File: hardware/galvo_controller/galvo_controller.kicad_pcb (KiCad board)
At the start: 4 copper layers, 75 x 95 mm, 134 parts, among them J1 USB_OTG, J2 Conn_01x03, J3 Conn_01x03, J4 Micro_SD_Card_Det, J5 Red, J6 White, J7 Conn_01x03, J8 Conn_01x03, Q1 MMBT2222, Q2 MMBT2222, SW1 JS1400BFQ, U1 SN74LV1T34, U10 LME49724, U2 UG-2832HSWEG02, U3 CP2104, U4 ESP-WROOM-32D, U5 TPS54295PWP, U6 PCM3060, U7 NCP1117LP, U8 OPA2134, U9 LME49724

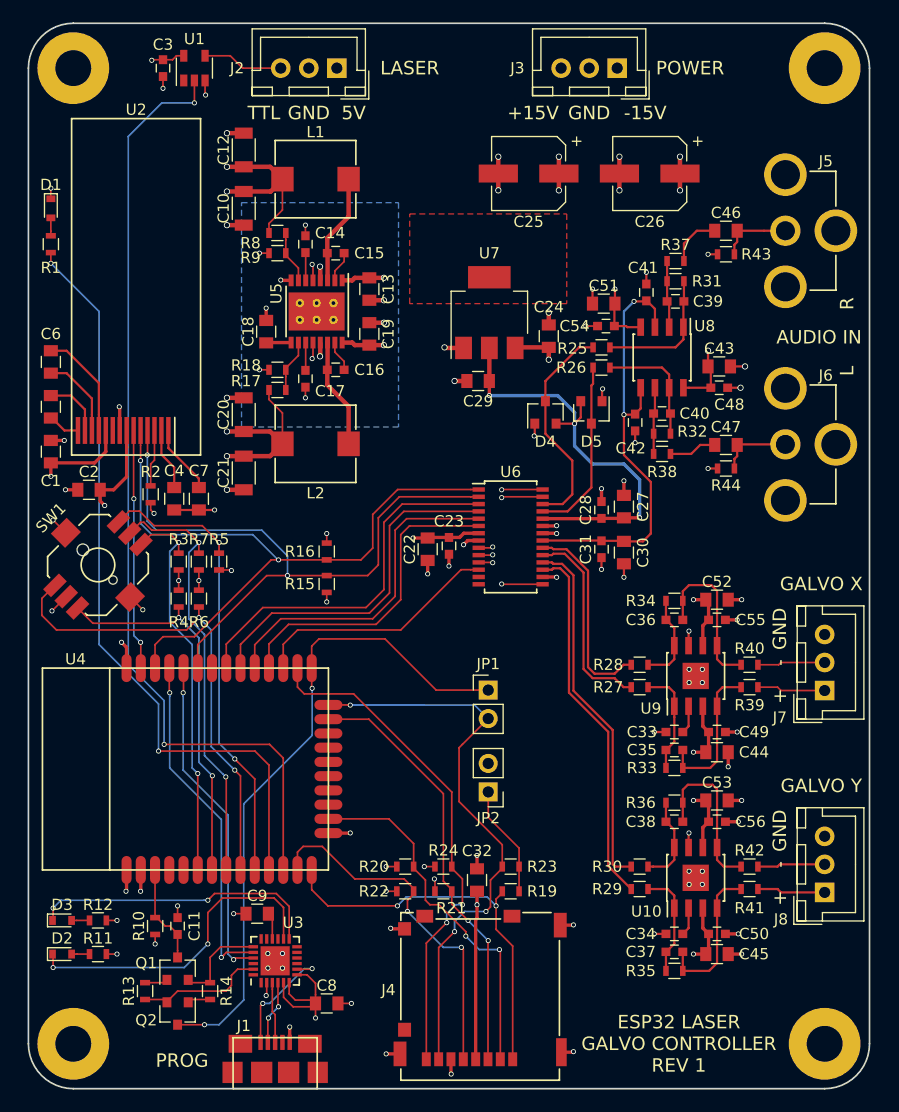
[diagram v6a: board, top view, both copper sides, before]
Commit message: Changed power connector.  Added symbols
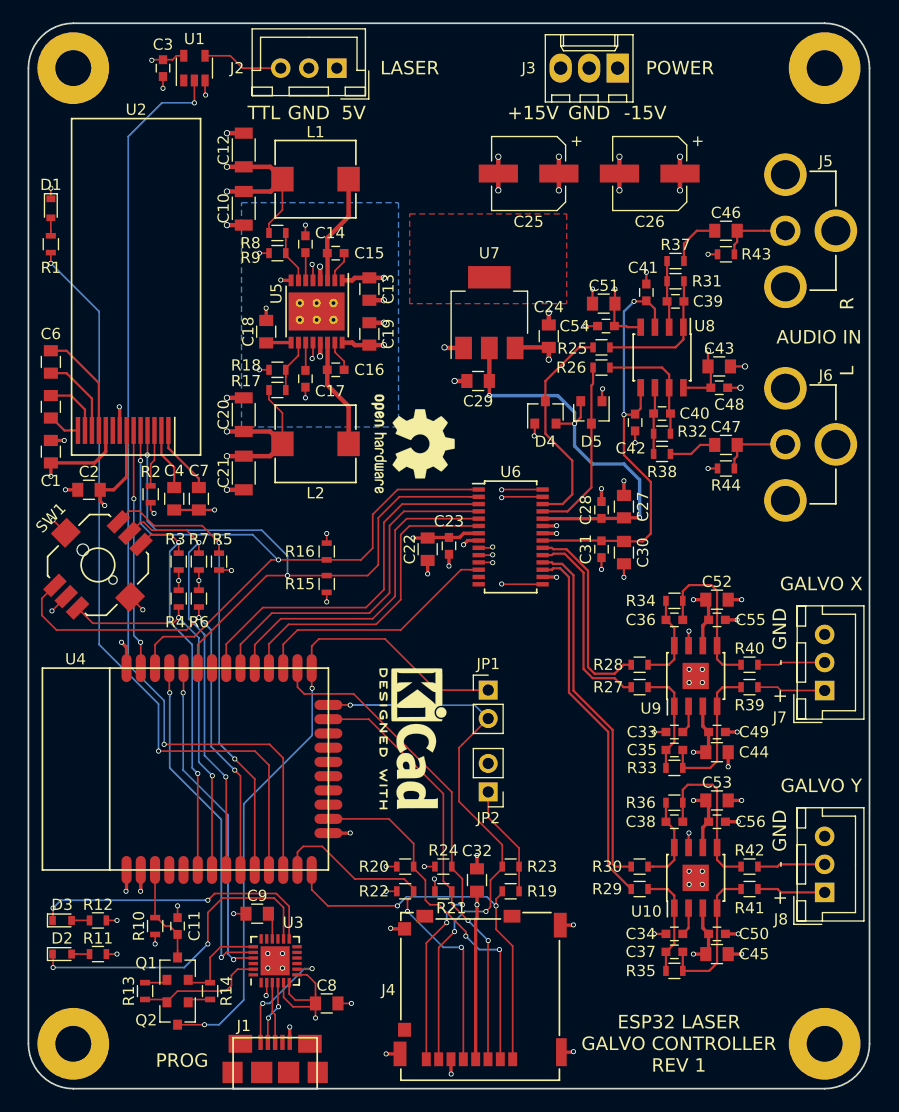
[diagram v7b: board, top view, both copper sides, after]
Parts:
- added REF***: KiCad-Logo2_6mm_SilkScreen, Symbols:KiCad-Logo2_6mm_SilkScreen, F.Cu at (169.3, 103.8)
- added REF***: OSHW-Logo2_7.3x6mm_SilkScreen, Symbols:OSHW-Logo2_9.8x8mm_SilkScreen, F.Cu at (169.3, 77.5)
- J3: footprint Connectors_JST:JST_XH_B03B-XH-A_03x2.50mm_Straight -> Connectors_Molex:Molex_KK-6410-03_03x2.54mm_Straight

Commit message: Fixed connector pinouts, working on silkscreen layers
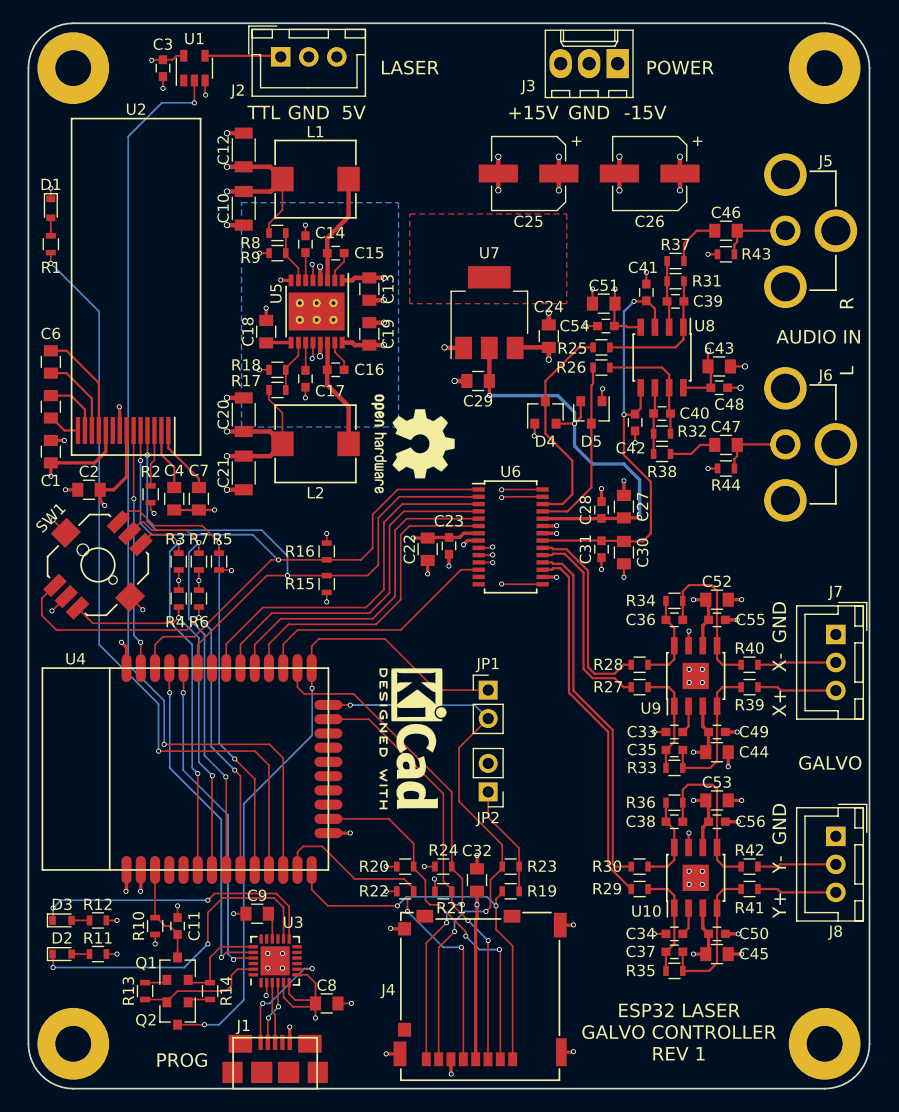
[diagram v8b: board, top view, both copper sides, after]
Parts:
- moved J2 5.10 mm to (157.5, 43.0), turned to 0 degrees
- moved J7 5.10 mm to (207.0, 94.5), turned to 270 degrees
- moved J8 5.10 mm to (207.0, 112.5), turned to 270 degrees
- moved J3 0.40 mm to (187.5, 43.6)
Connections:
- J2 pad 1: +5VD -> Net-(J2-Pad1)
- J2 pad 3: Net-(J2-Pad3) -> +5VD
- J7 pad 1: /X_P -> GNDA
- J7 pad 3: GNDA -> /X_P
- J8 pad 1: /Y_P -> GNDA
- J8 pad 3: GNDA -> /Y_P
- U1 pad 4: Net-(J2-Pad3) -> Net-(J2-Pad1)
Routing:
- net Net-(J2-Pad3): track 7.21 -> 0.00 mm
- net Net-(J2-Pad1): track 0.00 -> 6.79 mm
- net /Y_P: track 6.07 -> 7.07 mm
- net /Y_N: track 6.03 -> 7.03 mm
- net /X_P: track 6.07 -> 7.07 mm
- net /X_N: track 6.03 -> 7.03 mm
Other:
- board text added: "ESP32 LASER GALVO CONTROLLER https://github.com/jeffkub/esp32-galvo"
- board text added: "GALVO"
- board text added: "X+"
- board text added: "X-"
- board text added: "Y+"
- board text added: "Y-"
- board text removed: "+"
- board text removed: "-"
- board text removed: "GALVO X"
- board text removed: "GALVO Y"
